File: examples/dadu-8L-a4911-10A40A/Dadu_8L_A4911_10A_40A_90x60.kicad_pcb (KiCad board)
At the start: 8 copper layers, 90 x 60 mm, 130 parts, among them J1 12V 입력, J2 DAP, J3 CAN, J4 모터 상, J5 홀, J6 UART, Q1 SQD50P04-09L, Q2 IAUC60N04S6N050H, Q3 IAUC60N04S6N050H, Q4 IAUC60N04S6N050H, U1 TPS54331, U2 AMS1117-3.3, U3 LM317, U4 TC364DP, U5 TPS3823-33, U6 TLE9251V, U7 A4911, Y1 20MHz

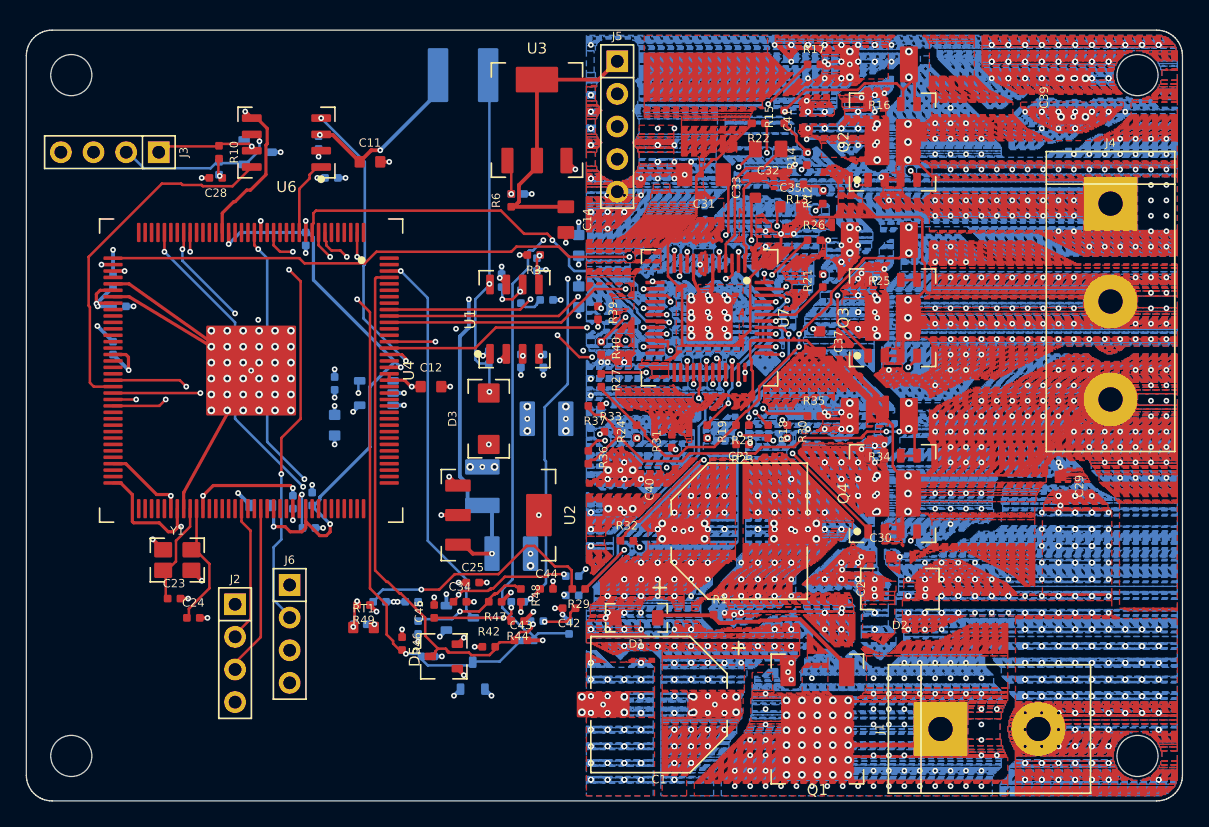
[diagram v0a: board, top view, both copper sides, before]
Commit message: v1.80.1: fine-pitch escape order (middle of a signal-pin run first); Dadu 10 A/40 A example fully routed
Co-Authored-By: Claude Opus 5.5 <noreply@anthropic.com>
Claude-Session: https://claude.ai/code/session_01ENBZQtx2ruaEBZiZmBjLaq
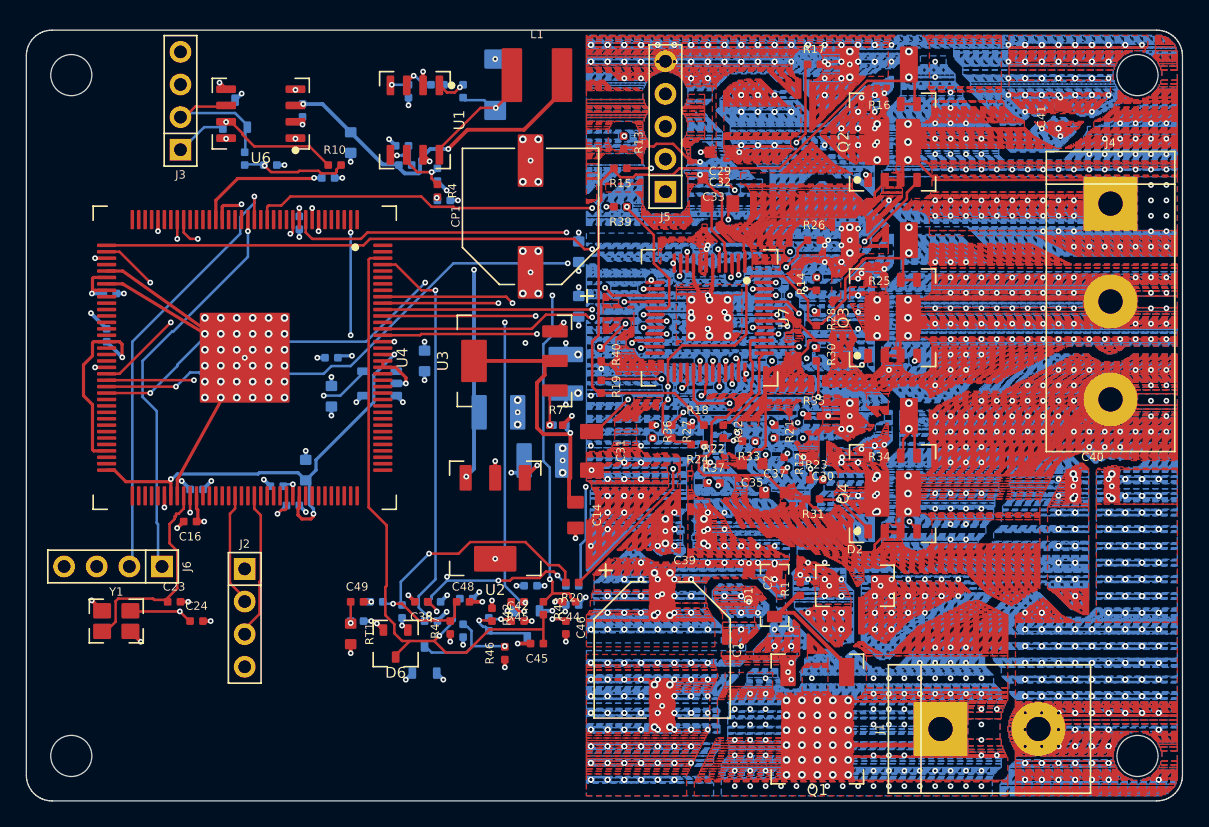
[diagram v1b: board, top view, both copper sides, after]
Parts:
- C11, C12, C25, C28, C34, C43, D3, D5, R29, R3, R44, R48, R49, R6: moved to B.Cu
- C16, C36, C46, C48, C49, D6, L1, R20, R4, R43, R45, R7: moved to F.Cu
- moved C39 45.3 mm to (76.2, 64.0), turned to 180 degrees
- moved C29 37.1 mm to (79.0, 34.5), turned to 180 degrees
- moved C40 36.8 mm to (108.0, 60.5), turned to 0 degrees
- moved CP1 29.4 mm to (64.2, 39.5), turned to 90 degrees
- moved R22 26.7 mm to (78.5, 58.8), turned to 0 degrees
- moved D3 26.0 mm to (61.5, 29.2)
- moved C8 23.5 mm to (54.8, 29.8)
- moved C31 23.2 mm to (69.0, 57.8), turned to 270 degrees
- moved C14 23.0 mm to (67.8, 62.8)
- moved R5 22.5 mm to (57.0, 29.2), turned to 0 degrees
- moved R12 21.0 mm to (84.0, 58.8), turned to 270 degrees
- moved C3 20.8 mm to (59.0, 29.8)
- moved C35 20.2 mm to (81.5, 58.8), turned to 180 degrees
- moved C41 19.8 mm to (105.5, 31.8)
- moved U3 18.8 mm to (63.0, 50.8), turned to 90 degrees
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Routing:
- net PH_U_HG: track 5.68 -> 47.5 mm, vias 2 -> 3
- net PH_V: track 75.8 -> 47.8 mm, vias 73 -> 76
- net +9V: track 21.5 -> 44.7 mm, vias 0 -> 1
- net PH_SDO: track 0.00 -> 21.6 mm, vias 0 -> 2
- net PH_U_LG: track 12.5 -> 30.2 mm, vias 2 -> 4
- net PH_W_LO: track 23.3 -> 7.16 mm, vias 2 -> 0
- net PH_W_LG: track 35.6 -> 20.4 mm
- net BUCK_SW: track 26.1 -> 12.1 mm, vias 2 -> 1
- net PH_HALL_B: track 40.0 -> 52.0 mm, vias 3 -> 1
- net PH_U: track 41.7 -> 51.9 mm, vias 80 -> 89
- net PH_U_SNS: track 49.8 -> 59.5 mm, vias 6 -> 2
- net PH_W_VB: track 4.71 -> 14.1 mm
- net VMON: track 54.4 -> 45.7 mm
- net PH_VREG: track 9.81 -> 18.4 mm
- net XTAL1: track 8.10 -> 16.5 mm
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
